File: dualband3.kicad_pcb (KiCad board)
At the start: 2 copper layers, 99.6 x 50.2 mm, 66 parts, among them J1 Conn_01x03_Male, J2 Conn_01x03_Male, J3 Conn_01x10_Male, J4 Conn_01x03_Male, J5 Conn_01x02_Male, J6 Conn_01x10_Male, J7 Conn_01x01_Male, P1 AD8402ARUZ1, SW1 SW_Push, U1 LD1117V33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

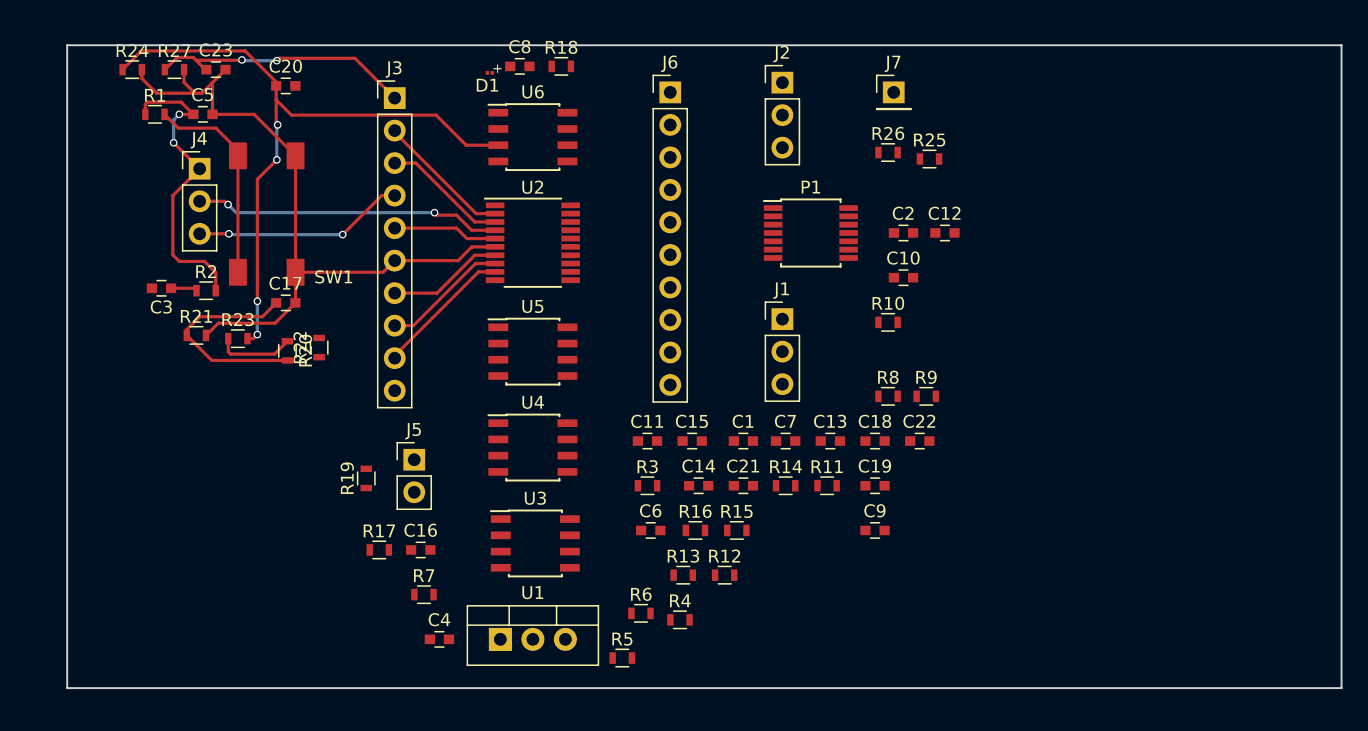
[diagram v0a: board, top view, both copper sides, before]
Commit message: Recreates PCB based on new layout
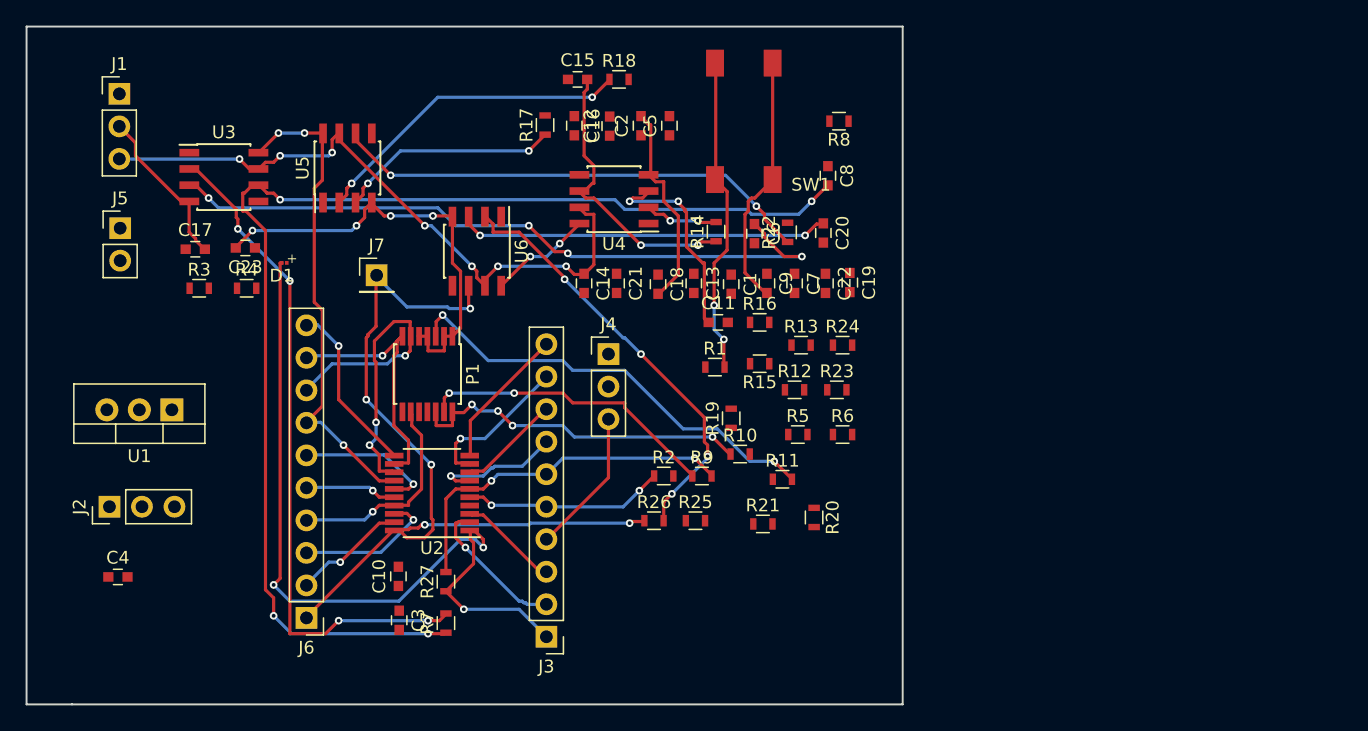
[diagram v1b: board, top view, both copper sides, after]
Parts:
- moved J2 62.1 mm to (115.7, 129.1), turned to 90 degrees
- moved R24 59.5 mm to (173.0, 116.5)
- moved J1 54.7 mm to (116.5, 96.9)
- moved J6 49.9 mm to (131.1, 137.8), turned to 180 degrees
- moved R1 48.0 mm to (163.0, 118.2)
- moved R23 47.0 mm to (172.5, 120.0)
- moved R21 46.6 mm to (166.8, 130.5)
- moved C10 45.8 mm to (138.3, 134.6), turned to 90 degrees
- moved R27 45.3 mm to (142.0, 135.0), turned to 90 degrees
- moved J3 43.7 mm to (149.8, 139.3), turned to 180 degrees
- moved C20 43.5 mm to (171.5, 107.8), turned to 270 degrees
- moved R20 43.2 mm to (170.8, 130.0)
- moved J7 42.9 mm to (136.6, 111.1)
- moved R4 42.6 mm to (126.4, 112.1)
- moved R2 38.6 mm to (159.0, 126.7)
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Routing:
- net Net-(C8-Pad2): track 0.00 -> 96.4 mm, vias 0 -> 4
- net /DataOut: track 0.00 -> 66.0 mm, vias 0 -> 5
- net GND: track 57.1 -> 112.4 mm, vias 0 -> 6
- net Net-(C6-Pad1): track 0.00 -> 55.1 mm, vias 0 -> 4
- net Net-(R7-Pad2): track 0.00 -> 52.8 mm, vias 0 -> 4
- net /~SD: track 0.00 -> 46.4 mm, vias 0 -> 5
- net +9V: track 6.14 -> 51.9 mm, vias 0 -> 7
- net Net-(C23-Pad1): track 21.0 -> 61.8 mm, vias 2 -> 3
- net Net-(C20-Pad2): track 0.00 -> 37.9 mm, vias 0 -> 2
- net Net-(P1-Pad3): track 0.00 -> 34.5 mm, vias 0 -> 2
- net Net-(R25-Pad1): track 0.00 -> 33.9 mm, vias 0 -> 4
- net Net-(J6-Pad8): track 0.00 -> 27.2 mm, vias 0 -> 3
- net Net-(P1-Pad12): track 0.00 -> 27.2 mm, vias 0 -> 4
- net Net-(R18-Pad1): track 0.00 -> 25.6 mm, vias 0 -> 2
- net Net-(C20-Pad1): track 53.8 -> 29.1 mm, vias 4 -> 2
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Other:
- board size 99.6 x 50.2 mm -> 68.5 x 53 mm
